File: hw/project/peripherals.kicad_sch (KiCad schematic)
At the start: 32 parts, among them J1 XT60PW-M, J2 Hall, J3 SWD, J4 Serial, J5 7461001, J6 7461001, J7 7461001

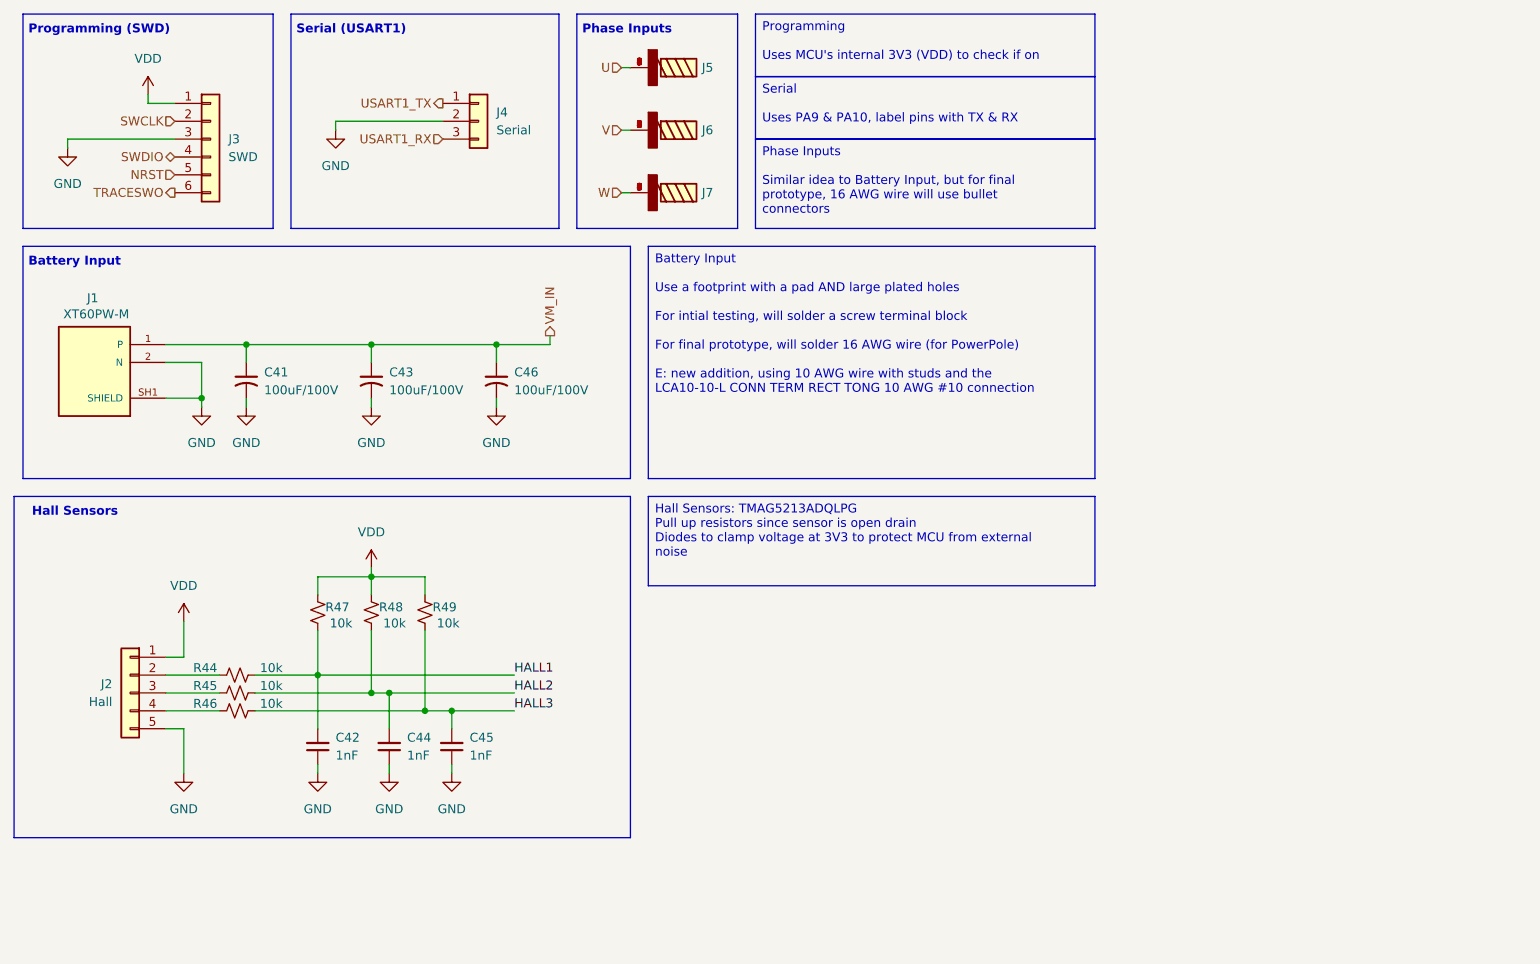
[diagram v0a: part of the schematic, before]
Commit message: Remove spec'd diodes and replace with original suggested parts
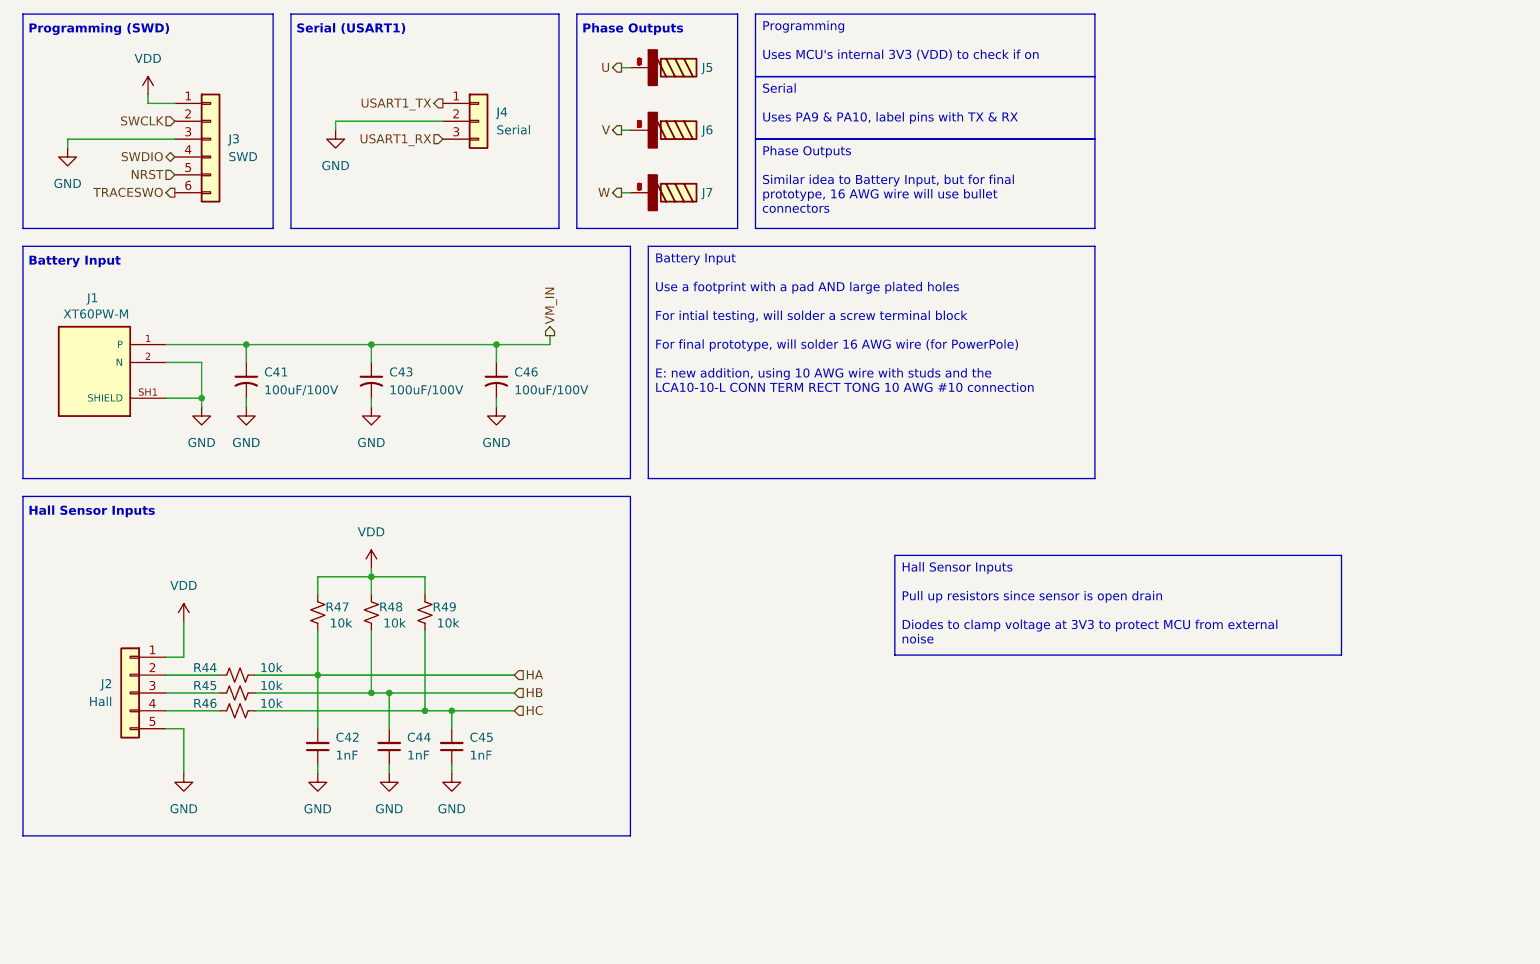
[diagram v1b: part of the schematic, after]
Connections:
- net HALL1 renamed HA
- net HALL2 renamed HB
- net HALL3 renamed HC
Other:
- note added: "Hall Sensor Inputs"
- note added: "Phase Outputs"
- note removed: "Hall Sensors"
- note removed: "Phase Inputs"
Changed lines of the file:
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@@
-	)
-	(rectangle
-		(start 13.97 86.36)
-		(end 101.6 134.874)
-		(stroke
-			(width 0)
-			(type default)
-		)
-		(fill
-			(type none)
-		)
 	)
 	(rectangle
@@
 		)
 	)
+	(rectangle
+		(start 15.24 86.36)
+		(end 101.6 134.62)
+		(stroke
+			(width 0)
+			(type default)
+		)
+		(fill
+			(type none)
+		)
+	)
 	(text "Battery Input"
 		(exclude_from_sim no)
@@
 		)
 	)
-	(text "Hall Sensors"
-		(exclude_from_sim no)
-		(at 16.51 87.884 0)
+	(text "Hall Sensor Inputs"
+		(exclude_from_sim no)
+		(at 16.002 87.884 0)
 		(effects
 			(font
@@
 		)
 	)
-	(text "Phase Inputs"
+	(text "Phase Outputs"
 		(exclude_from_sim no)
 		(at 94.742 19.304 0)
@@
 		)
 	)
-	(text_box "Hall Sensors: TMAG5213ADQLPG\nPull up resistors since sensor is open drain\nDiodes to clamp voltage at 3V3 to protect MCU from external noise\n"
-		(exclude_from_sim no)
-		(at 104.14 86.36 0)
-		(size 63.5 12.7)
+	(text_box "Hall Sensor Inputs\n\nPull up resistors since sensor is open drain\n\nDiodes to clamp voltage at 3V3 to protect MCU from external noise\n"
+		(exclude_from_sim no)
+		(at 139.192 94.742 0)
+		(size 63.5 14.1714)
 		(margins 0.9525 0.9525 0.9525 0.9525)
 		(stroke
@@
 		)
 	)
-	(text_box "Phase Inputs\n\nSimilar idea to Battery Input, but for final prototype, 16 AWG wire will use bullet connectors"
+	(text_box "Phase Outputs\n\nSimilar idea to Battery Input, but for final prototype, 16 AWG wire will use bullet connectors"
 		(exclude_from_sim no)
 		(at 119.38 35.56 0)
@@
 		)
 	)
-	(label "HALL1"
-		(at 85.09 111.76 0)
-		(effects
-			(font
-				(size 1.27 1.27)
-			)
-			(justify left bottom)
-		)
-	)
-	(label "HALL2"
-		(at 85.09 114.3 0)
-		(effects
-			(font
-				(size 1.27 1.27)
-			)
-			(justify left bottom)
-		)
-	)
-	(label "HALL3"
+	(hierarchical_label "HC"
+		(shape input)
 		(at 85.09 116.84 0)
 		(effects
@@
 				(size 1.27 1.27)
 			)
-			(justify left bottom)
+			(justify left)
 		)
 	)
 	(hierarchical_label "V"
-		(shape input)
+		(shape output)
 		(at 100.33 34.29 180)
 		(effects
@@
 	)
 	(hierarchical_label "U"
-		(shape input)
+		(shape output)
 		(at 100.33 25.4 180)
 		(effects
@@
 	)
 	(hierarchical_label "W"
+		(shape output)
+		(at 100.33 43.18 180)
+		(effects
+			(font
+				(size 1.27 1.27)
+			)
+			(justify right)
+		)
+	)
+	(hierarchical_label "HB"
 		(shape input)
-		(at 100.33 43.18 180)
-		(effects
-			(font
-				(size 1.27 1.27)
-			)
-			(justify right)
+		(at 85.09 114.3 0)
+		(effects
+			(font
+				(size 1.27 1.27)
+			)
+			(justify left)
 		)
 	)
@@
 		)
 	)
+	(hierarchical_label "HA"
+		(shape input)
+		(at 85.09 111.76 0)
+		(effects
+			(font
+				(size 1.27 1.27)
+			)
+			(justify left)
+		)
+	)

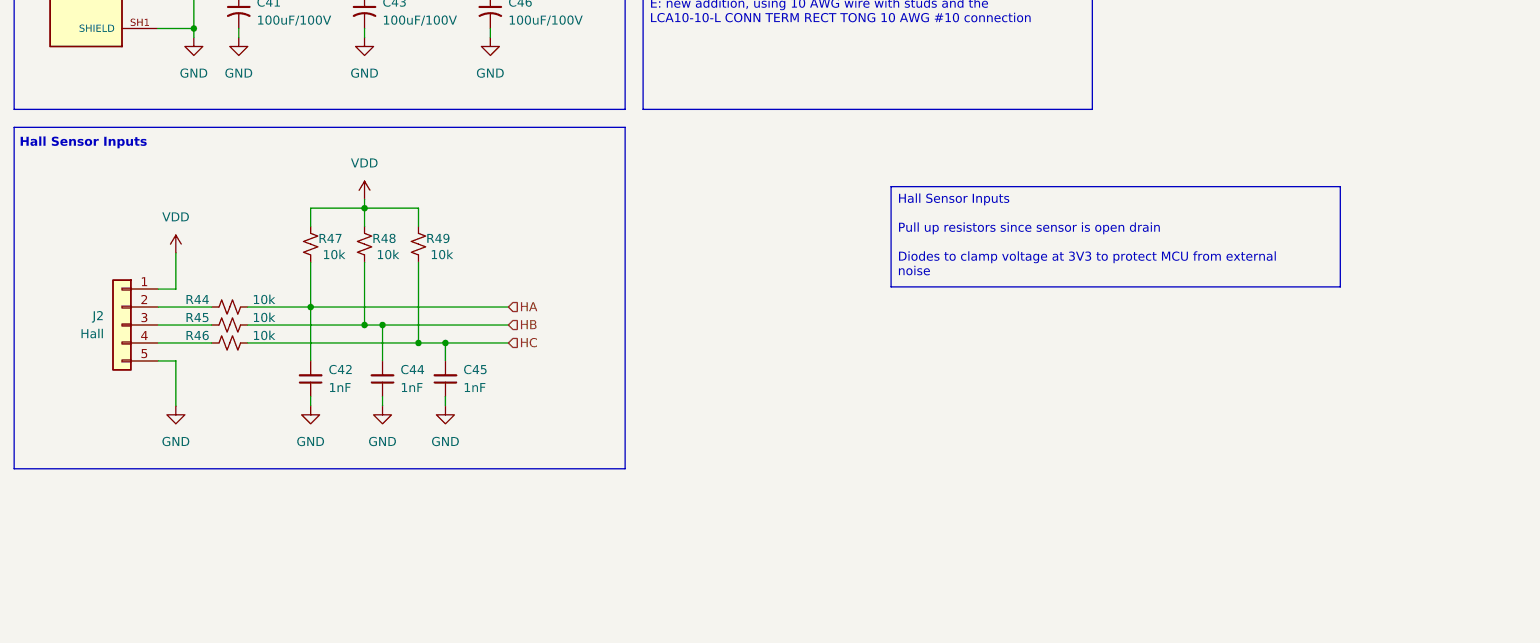
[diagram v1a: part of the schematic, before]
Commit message: Revise hall sensor inputs
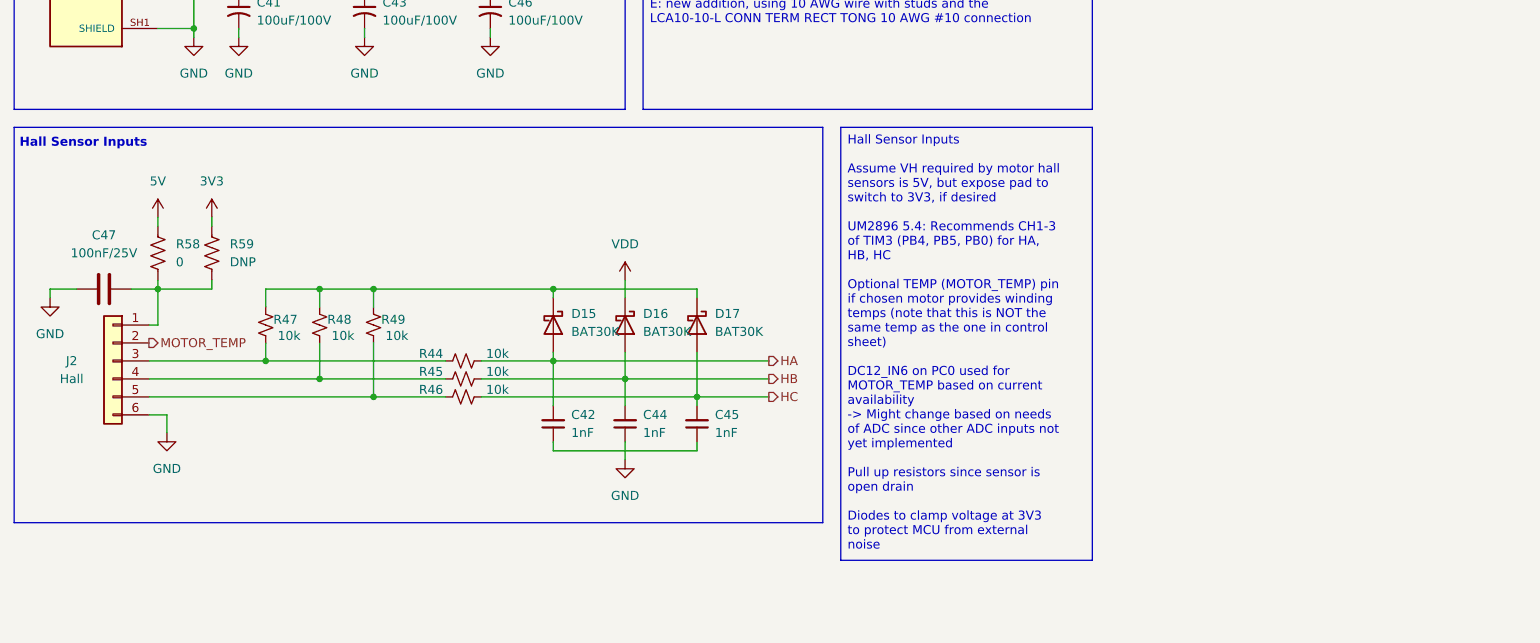
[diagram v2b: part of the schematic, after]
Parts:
- added C47: 100nF/25V, symbol Device:C
- added D15, D16, D17: BAT30K, symbol Device:D_Schottky
- added R58: 0, symbol Device:R_US
- added R59: DNP, symbol Device:R_US
- J2: symbol Connector_Generic:Conn_01x05 -> Connector_Generic:Conn_01x06
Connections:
- net GND: now also J2.6 (Pin_6), C47.2; no longer C42.1, C45.1, J2.5 (Pin_5)
- net HA: now also D15.2 (A); no longer R47.1
- net HB: now also D16.2 (A); no longer R48.1
- net HC: now also D17.2 (A); no longer R49.1
- net VDD: now also D16.1 (K); no longer J2.1 (Pin_1), R47.2, R48.2, R49.2
- net at R45.1: now also J2.4 (Pin_4), R48.1; no longer J2.3 (Pin_3)
- net at R44.1: now also J2.3 (Pin_3), R47.1; no longer J2.2 (Pin_2)
- net at R46.1: now also J2.5 (Pin_5), R49.1; no longer J2.4 (Pin_4)
- new net: D15.1 (K), D17.1 (K), R47.2, R48.2, R49.2
- new net: C47.1, J2.1 (Pin_1), R58.2, R59.2
- new net: C42.1, C45.1
- new net 3V3: R59.1
- new net 5V: R58.1
- new net MOTOR_TEMP: J2.2 (Pin_2)
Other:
- moved on the sheet: C42, C44, C45, R44, R45, R46, R47, R48, R49

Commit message: Set up last bit of HW tasks
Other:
- note added: "ADC Inputs"
- note added: "LEDs"
- note added: "Misc Pins????"
- note added: "Secondary Headers???"
- note added: "Switches"
- note added: "Trimming"
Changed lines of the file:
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@@
 	(paper "A4")
+	(rectangle
+		(start 209.296 95.25)
+		(end 244.856 125.73)
+		(stroke
+			(width 0)
+			(type default)
+		)
+		(fill
+			(type none)
+		)
+	)
+	(rectangle
+		(start 15.24 147.32)
+		(end 50.8 177.8)
+		(stroke
+			(width 0)
+			(type default)
+		)
+		(fill
+			(type none)
+		)
+	)
 	(rectangle
 		(start 251.46 19.05)
@@
 	)
 	(rectangle
+		(start 53.34 147.32)
+		(end 88.9 177.8)
+		(stroke
+			(width 0)
+			(type default)
+		)
+		(fill
+			(type none)
+		)
+	)
+	(rectangle
 		(start 15.24 50.8)
 		(end 101.6 83.82)
@@
 	)
 	(rectangle
+		(start 129.54 152.146)
+		(end 165.1 182.626)
+		(stroke
+			(width 0)
+			(type default)
+		)
+		(fill
+			(type none)
+		)
+	)
+	(rectangle
 		(start 15.24 17.78)
 		(end 50.8 48.26)
@@
 		)
 	)
+	(rectangle
+		(start 180.848 131.572)
+		(end 216.408 162.052)
+		(stroke
+			(width 0)
+			(type default)
+		)
+		(fill
+			(type none)
+		)
+	)
+	(rectangle
+		(start 91.44 147.32)
+		(end 127 177.8)
+		(stroke
+			(width 0)
+			(type default)
+		)
+		(fill
+			(type none)
+		)
+	)
 	(text "Battery Input"
 		(exclude_from_sim no)
@@
 		)
 	)
+	(text "Trimming"
+		(exclude_from_sim no)
+		(at 16.002 148.844 0)
+		(effects
+			(font
+				(size 1.27 1.27)
+				(thickness 0.254)
+				(bold yes)
+			)
+			(justify left top)
+		)
+	)
+	(text "Switches"
+		(exclude_from_sim no)
+		(at 54.102 148.844 0)
+		(effects
+			(font
+				(size 1.27 1.27)
+				(thickness 0.254)
+				(bold yes)
+			)
+			(justify left top)
+		)
+	)
+	(text "ADC Inputs"
+		(exclude_from_sim no)
+		(at 130.302 153.67 0)
+		(effects
+			(font
+				(size 1.27 1.27)
+				(thickness 0.254)
+				(bold yes)
+			)
+			(justify left top)
+		)
+	)
 	(text "Programming (SWD)"
 		(exclude_from_sim no)
@@
 		)
 	)
+	(text "LEDs"
+		(exclude_from_sim no)
+		(at 92.202 148.844 0)
+		(effects
+			(font
+				(size 1.27 1.27)
+				(thickness 0.254)
+				(bold yes)
+			)
+			(justify left top)
+		)
+	)
 	(text "Hall Sensor Inputs"
 		(exclude_from_sim no)
@@
 		)
 	)
+	(text "Secondary Headers???"
+		(exclude_from_sim no)
+		(at 210.058 96.774 0)
+		(effects
+			(font
+				(size 1.27 1.27)
+				(thickness 0.254)
+				(bold yes)
+			)
+			(justify left top)
+		)
+	)
 	(text "Phase Outputs"
 		(exclude_from_sim no)
@@
 		(effects
 			(font
+				(size 1.27 1.27)
+				(thickness 0.254)
+				(bold yes)
+			)
+			(justify left top)
+		)
+	)
+	(text "Misc Pins????"
+		(exclude_from_sim no)
+		(at 181.61 133.096 0)
+		(effects
+			(font

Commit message: Prep remaining tasks and show CAN + trimmer
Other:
- note added: "CAN"
- note added: "I2C?"
- note added: "SPI?"
- note added: "Speed Trimmer"
- note added: "Status LEDs -> REDO!!!"
- note added: "User Switch & LED"
- note added: "Voltage Monitor"
- note removed: "LEDs"
- note removed: "Status LEDs -> re-do?"
- note removed: "Switches"
- note removed: "Trimming"
- moved on the sheet: D10, D11, D12, D13, D9, R50, R51, R52, R53, R54, R55, R56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

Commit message: can tranceiver
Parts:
- added C48: CAP ALUM 22UF 20% 16V SMD, footprints:CP_Wurth_WCAP-ASLI-D4L5.5, symbol symbols:D4L5.5_865080340003
- added C49, C51: CAP CER 0.1UF 25V X7R 0603, Capacitor_SMD:C_0603_1608Metric, symbol Device:C_Small
- added C50: CAP CER 0603 4.7NF 16V X7R 10%, Capacitor_SMD:C_0603_1608Metric, symbol Device:C_Small
- added D18, D2: TVS DIODE 5VWM 12.5VC SOD-523, footprints:P38_SOD-523, symbol symbols:Diode
- added J8: CONN HEADER VERT 4POS 2.5MM, footprints:CONN_B4B-XH-A_JST, symbol symbols:B4B-XH-A
- added R60, R61: RES 60.4 OHM 1% 1/10W 0603, Resistor_SMD:R_0603_1608Metric, symbol Device:R_Small_US
- added TP8, TP9: TestPoint, TestPoint:TestPoint_Pad_D1.0mm, symbol Connector:TestPoint
- added U5: IC TRANSCEIVER 1/1 8SO, footprints:SOIC8_4P9X3P9MC_MCH, symbol symbols:ATA6561-GAQW-N
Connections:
- net 3V3: now also C51.1, U5.5 (VIO)
- net 5V: now also C48.1, C49.1, U5.1 (TXD)
- net GND: now also C48.2, C49.2, C50.2, C51.2, D18.1 (A), D2.1 (A), J8.4, U5.4 (RXD)
- new net: C50.1, R60.2, R61.1
- new net CAN_N: D18.2 (C), J8.3, R61.2, TP9.1, U5.6 (CANL)
- new net CAN_P: D2.2 (C), J8.2, R60.1, TP8.1, U5.7 (CANH)
- new net RXD: U5.3 (VCC)
- new net STBY: U5.8 (STBY)
- new net TXD: U5.2 (GND)
- no-connect marks 0 -> 1
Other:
- note added: "C = 1/2piRf = 5.3nF -> 4.7nF f = 500kHz R = 60.4"
- note added: "CAN Tranceiver"
- note added: "CANBus Split Termination (see datasheet)"
- note added: "CANBus connection to other boards"

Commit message: speed trimmer and leds
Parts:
- removed C48: CAP ALUM 22UF 20% 16V SMD, footprints:CP_Wurth_WCAP-ASLI-D4L5.5, symbol symbols:D4L5.5_865080340003
- removed J8: CONN HEADER VERT 4POS 2.5MM, footprints:CONN_B4B-XH-A_JST, symbol symbols:B4B-XH-A
- removed U5: IC TRANSCEIVER 1/1 8SO, footprints:SOIC8_4P9X3P9MC_MCH, symbol symbols:ATA6561-GAQW-N
- added C52: 33nF, Capacitor_SMD:C_0603_1608Metric, symbol Device:C_Small
- added C53, C54: 1nF, Capacitor_SMD:C_0603_1608Metric, symbol Device:C_Small
- added C55: 22uF, WCAP-ASLI_4X5.5:WCAP-ASLI_4X5.5_DXL_, symbol WCAP-ASLI_4X5.5:WCAP-ASLI_4X5.5
- added D19, D20, D21, D22, D23, D24, D25, D26, D27, D28: 2Vf, LED_SMD:LED_0603_1608Metric_Pad1.05x0.95mm_HandSolder, symbol Device:LED
- added J9: CONN HEADER VERT 4POS 2.5MM, Connector_JST:JST_XH_B4B-XH-A_1x04_P2.50mm_Vertical, symbol Connector_Generic:Conn_01x04
- added R70: 0, symbol Device:R_Small_US
- added R71, R74: 100k, symbol Device:R_Small_US
- added R72, R75: 120, symbol Device:R_Small_US
- added R73, R76: 200, symbol Device:R_Small_US
- added R77, R78: 2320, symbol Device:R_Small_US
- added R79, R80, R81, R83, R84, R85: 130, symbol Device:R_Small_US
- added R82: 300, symbol Device:R_Small_US
- added RV1: R_Potentiometer_US, symbol Device:R_Potentiometer_US
- added SW3, SW4: RESET, SWT0220_016016GSA:SW_SWT0220-016016GSA_REVA, symbol Switch:SW_Push
- added TP10: SPEED, TestPoint:TestPoint_Pad_D1.0mm, symbol Connector:TestPoint
- added U2: ATA6561-GAQW-N, ATA6561_GAQW_N:SOIC8_4P9X3P9MC_MCH, symbol ATA6561_GAQW_N:ATA6561-GAQW-N
- C49, C51: value CAP CER 0.1UF 25V X7R 0603 -> 0.1uF
- D18, D2: footprint footprints:P38_SOD-523 -> Diode_SMD:D_SOD-523
- TP8: value TestPoint -> CANP
- TP9: value TestPoint -> CANN
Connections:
- net 3V3: now also C51.2, R80.2, R81.2, RV1.1, SW3.1, SW4.1, U2.5 (VIO); no longer C51.1
- net 5V: now also C49.2, C55.1, R82.2, U2.1 (TXD); no longer C49.1
- net CAN_N: now also J9.3 (Pin_3), U2.6 (CANL)
- net CAN_P: now also J9.2 (Pin_2), U2.7 (CANH)
- net FAULT: now also D21.1 (K)
- net GND: now also C49.1, C51.1, C52.1, C53.1, C54.1, C55.2, D19.1 (K), D20.1 (K), D22.1 (K), D23.1 (K), D24.1 (K), D25.1 (K), D26.1 (K), D27.1 (K), D28.1 (K), J9.4 (Pin_4), R71.1, R74.1, RV1.3, U2.4 (RXD); no longer C49.2, C51.2
- net RXD: now also U2.3 (VCC)
- net STBY: now also U2.8 (STBY)
- net TXD: now also U2.2 (GND)
- net VM: now also R77.2
- new net: D27.2 (A), R84.1
- new net: D21.2 (A), R80.1
- new net: D26.2 (A), R83.1
- new net: C54.2, R74.2, R75.2, R76.2, SW4.2
- new net: D22.2 (A), R79.1
- new net: D28.2 (A), R85.1
- new net: C53.2, R71.2, R72.2, R73.2, SW3.2
- new net: D19.2 (A), R82.1
- new net: D25.2 (A), R75.1
- new net: D20.2 (A), R81.1
- new net: D23.2 (A), R78.1
- new net: R77.1, R78.2
- new net: C52.2, R70.1, RV1.2, TP10.1
- new net: D24.2 (A), R72.1
- new net BTN: R76.1
- new net LED1: R84.2
- new net LED2: R85.2
- new net SPEED: R70.2
- new net STATUS1: R79.2
- new net STATUS2: R83.2
- new net USER/WAKE: R73.1
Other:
- note added: "10mA LEDs, 20mA max"
- note added: "Extra leds can be used for rx/tx or whatever"
- note added: "evspin had two of these, one for wake and another for idk what"
- note added: "we should expose all data lines with headers that will make it easier for fw to test (other than can) also we could probably do with some more test opints"

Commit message: Reorg CAN
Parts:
- removed D10, D11, D12, D13, D9: 2Vf, LED_SMD:LED_0603_1608Metric_Pad1.05x0.95mm_HandSolder, symbol Device:LED
- removed R50: 200, symbol Device:R_US
- removed R51, R52, R53: 91, symbol Device:R_US
- removed R54, R55, R56, R57: 2.4k, symbol Device:R_US
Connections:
- net 5V: now also U2.3 (VCC); no longer U2.1 (TXD)
- net GND: now also U2.2 (GND); no longer U2.4 (RXD)
- net RXD: now also U2.4 (RXD); no longer U2.3 (VCC)
- net TXD: now also U2.1 (TXD); no longer U2.2 (GND)
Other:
- note added: "CAN Transceiver"
- note added: "CANBus Connector"
- note added: "CANBus Split Termination"
- note removed: "CAN"
- note removed: "CAN Tranceiver"
- note removed: "CANBus Split Termination (see datasheet)"
- note removed: "CANBus connection to other boards"
- note removed: "Status LEDs -> REDO!!!"
- moved on the sheet: C49, C50, C51, C55, D18, D2, J9, R60, R61, TP8, TP9, U2
